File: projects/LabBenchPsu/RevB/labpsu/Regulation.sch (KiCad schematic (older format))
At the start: 19 parts

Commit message: schematic more or less done
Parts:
- IC4: renamed from IC?; footprint SparkFun-SO08 -> (none)
- Q2, Q3: renamed from Q?; footprint TO92 -> (none)
- gave numbers to parts that had none: 15
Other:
- note added: "0-2V V_set \n(for 0-20V V_out)"
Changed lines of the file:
@@
 $EndDescr
 $Comp
-L LT3083 U?
+L LT3083 U9
 U 1 1 57EF9BBB
 P 7075 2450
-F 0 "U?" H 7075 2875 60  0000 C CNN
+F 0 "U9" H 7075 2875 60  0000 C CNN
 F 1 "LT3083" H 7075 2775 60  0000 C CNN
-F 2 "" H 7075 2450 60  0000 C CNN
+F 2 "" H 7075 2450 60  0001 C CNN
 F 3 "" H 7075 2450 60  0000 C CNN
 	1    7075 2450
@@
 NoConn ~ 7650 2325
 $Comp
-L DIODESCH D?
+L DIODESCH D2
 U 1 1 57EF9BC4
 P 7100 1750
-F 0 "D?" H 7100 1850 40  0000 C CNN
+F 0 "D2" H 7100 1850 40  0000 C CNN
 F 1 "SK33A" H 7100 1650 40  0000 C CNN
-F 2 "" H 7100 1750 60  0000 C CNN
+F 2 "" H 7100 1750 60  0001 C CNN
 F 3 "" H 7100 1750 60  0000 C CNN
 	1    7100 1750
@@
 P 4800 3350
 AR Path="/57EF9BF5" Ref="IC?"  Part="1"
-AR Path="/57EF8FB1/57EF9BF5" Ref="IC?"  Part="1"
-F 0 "IC?" H 5125 3250 50  0000 R TNN
+AR Path="/57EF8FB1/57EF9BF5" Ref="IC4"  Part="1"
+F 0 "IC4" H 5125 3250 50  0000 R TNN
 F 1 "LM358" H 4675 3400 50  0000 R TNN
-F 2 "SparkFun-SO08" H 4800 3500 50  0001 C CNN
+F 2 "" H 4800 3500 50  0001 C CNN
 F 3 "" H 4800 3350 60  0000 C CNN
 	1    4800 3350
@@
 P 4900 4425
 AR Path="/57EF9BFC" Ref="IC?"  Part="2"
-AR Path="/57EF8FB1/57EF9BFC" Ref="IC?"  Part="2"
-F 0 "IC?" H 5125 4325 50  0000 R TNN
+AR Path="/57EF8FB1/57EF9BFC" Ref="IC4"  Part="2"
+F 0 "IC4" H 5125 4325 50  0000 R TNN
 F 1 "LM358" H 5200 4575 50  0000 R TNN
-F 2 "SparkFun-SO08" H 4900 4575 50  0001 C CNN
+F 2 "" H 4900 4575 50  0001 C CNN
 F 3 "" H 4900 4425 60  0000 C CNN
 	2    4900 4425
@@
 $EndComp
 $Comp
-L GND #PWR?
+L GND #PWR060
 U 1 1 57EF9C03
 P 4800 3650
-F 0 "#PWR?" H 4800 3650 30  0001 C CNN
+F 0 "#PWR060" H 4800 3650 30  0001 C CNN
 F 1 "GND" H 4800 3580 30  0001 C CNN
 F 2 "" H 4800 3650 60  0000 C CNN
@@
 VSET
 $Comp
-L R R?
+L R R50
 U 1 1 57EF9C0B
 P 4350 2775
-F 0 "R?" V 4430 2775 40  0000 C CNN
+F 0 "R50" V 4430 2775 40  0000 C CNN
 F 1 "18K 0.1%" V 4357 2776 40  0000 C CNN
-F 2 "" V 4280 2775 30  0000 C CNN
+F 2 "" V 4280 2775 30  0001 C CNN
 F 3 "" H 4350 2775 30  0000 C CNN
 	1    4350 2775
@@
 $EndComp
 $Comp
-L R R?
+L R R49
 U 1 1 57EF9C12
 P 4350 2625
-F 0 "R?" V 4430 2625 40  0000 C CNN
+F 0 "R49" V 4430 2625 40  0000 C CNN
 F 1 "18K 0.1%" V 4357 2626 40  0000 C CNN
-F 2 "" V 4280 2625 30  0000 C CNN
+F 2 "" V 4280 2625 30  0001 C CNN
 F 3 "" H 4350 2625 30  0000 C CNN
 	1    4350 2625
@@
 $EndComp
 $Comp
-L R R?
+L R R48
 U 1 1 57EF9C19
 P 3850 2625
-F 0 "R?" V 3930 2625 40  0000 C CNN
+F 0 "R48" V 3930 2625 40  0000 C CNN
 F 1 "1K 0.1%" V 3857 2626 40  0000 C CNN
-F 2 "" V 3780 2625 30  0000 C CNN
+F 2 "" V 3780 2625 30  0001 C CNN
 F 3 "" H 3850 2625 30  0000 C CNN
 	1    3850 2625
@@
 $EndComp
 $Comp
-L GND #PWR?
+L GND #PWR061
 U 1 1 57EF9C20
 P 3600 2725
-F 0 "#PWR?" H 3600 2725 30  0001 C CNN
+F 0 "#PWR061" H 3600 2725 30  0001 C CNN
 F 1 "GND" H 3600 2655 30  0001 C CNN
 F 2 "" H 3600 2725 60  0000 C CNN
@@
 $EndComp
 $Comp
-L R R?
+L R R51
 U 1 1 57EF9C26
 P 5525 3350
-F 0 "R?" V 5605 3350 40  0000 C CNN
+F 0 "R51" V 5605 3350 40  0000 C CNN
 F 1 "1K" V 5532 3351 40  0000 C CNN
-F 2 "" V 5455 3350 30  0000 C CNN
+F 2 "" V 5455 3350 30  0001 C CNN
 F 3 "" H 5525 3350 30  0000 C CNN
 	1    5525 3350
@@
 $EndComp
 $Comp
-L R R?
+L R R54
 U 1 1 57EF9C2D
 P 6325 3350
-F 0 "R?" V 6405 3350 40  0000 C CNN
+F 0 "R54" V 6405 3350 40  0000 C CNN
 F 1 "100R" V 6332 3351 40  0000 C CNN
-F 2 "" V 6255 3350 30  0000 C CNN
+F 2 "" V 6255 3350 30  0001 C CNN
 F 3 "" H 6325 3350 30  0000 C CNN
 	1    6325 3350
@@
 $EndComp
 $Comp
-L R R?
+L R R52
 U 1 1 57EF9C34
 P 5525 3550
-F 0 "R?" V 5605 3550 40  0000 C CNN
+F 0 "R52" V 5605 3550 40  0000 C CNN
 F 1 "10K" V 5532 3551 40  0000 C CNN
-F 2 "" V 5455 3550 30  0000 C CNN
+F 2 "" V 5455 3550 30  0001 C CNN
 F 3 "" H 5525 3550 30  0000 C CNN
 	1    5525 3550
@@
 $EndComp
 $Comp
-L 2N3904 Q?
+L 2N3904 Q2
 U 1 1 57EF9C3B
 P 5975 3550
-F 0 "Q?" H 5975 3401 40  0000 R CNN
+F 0 "Q2" H 5975 3401 40  0000 R CNN
 F 1 "2N3904" H 6400 3550 40  0000 R CNN
-F 2 "TO92" H 5875 3652 29  0000 C CNN
+F 2 "" H 5875 3652 29  0001 C CNN
 F 3 "" H 5975 3550 60  0000 C CNN
 	1    5975 3550
@@
 $EndComp
 $Comp
-L GND #PWR?
+L GND #PWR062
 U 1 1 57EF9C42
 P 6075 3750
-F 0 "#PWR?" H 6075 3750 30  0001 C CNN
+F 0 "#PWR062" H 6075 3750 30  0001 C CNN
 F 1 "GND" H 6075 3680 30  0001 C CNN
 F 2 "" H 6075 3750 60  0000 C CNN
@@
 $EndComp
 $Comp
-L C C?
+L C C25
 U 1 1 57EF9C73
 P 5025 2975
-F 0 "C?" H 5025 3075 40  0000 L CNN
+F 0 "C25" H 5025 3075 40  0000 L CNN
 F 1 "100nF" H 5031 2890 40  0000 L CNN
-F 2 "" H 5063 2825 30  0000 C CNN
+F 2 "" H 5063 2825 30  0001 C CNN
 F 3 "" H 5025 2975 60  0000 C CNN
 	1    5025 2975
@@
 $EndComp
 $Comp
-L GND #PWR?
+L GND #PWR063
 U 1 1 57EF9C7A
 P 5025 3175
-F 0 "#PWR?" H 5025 3175 30  0001 C CNN
+F 0 "#PWR063" H 5025 3175 30  0001 C CNN
 F 1 "GND" H 5025 3105 30  0001 C CNN
 F 2 "" H 5025 3175 60  0000 C CNN
@@
 $EndComp
 $Comp
-L R R?
+L R R53
 U 1 1 57EF9C81
 P 5525 4425
-F 0 "R?" V 5605 4425 40  0000 C CNN
+F 0 "R53" V 5605 4425 40  0000 C CNN
 F 1 "10K" V 5532 4426 40  0000 C CNN
-F 2 "" V 5455 4425 30  0000 C CNN
+F 2 "" V 5455 4425 30  0001 C CNN
 F 3 "" H 5525 4425 30  0000 C CNN
 	1    5525 4425
@@
 $EndComp
 $Comp
-L 2N3904 Q?
+L 2N3904 Q3
 U 1 1 57EF9C88
 P 5975 4425
-F 0 "Q?" H 5975 4276 40  0000 R CNN
+F 0 "Q3" H 5975 4276 40  0000 R CNN
 F 1 "2N3904" H 6400 4425 40  0000 R CNN
-F 2 "TO92" H 5875 4527 29  0000 C CNN
+F 2 "" H 5875 4527 29  0001 C CNN
 F 3 "" H 5975 4425 60  0000 C CNN
 	1    5975 4425
@@
 $EndComp
 $Comp
-L GND #PWR?
+L GND #PWR064
 U 1 1 57EF9C8F
 P 6075 4625
-F 0 "#PWR?" H 6075 4625 30  0001 C CNN
+F 0 "#PWR064" H 6075 4625 30  0001 C CNN
 F 1 "GND" H 6075 4555 30  0001 C CNN
 F 2 "" H 6075 4625 60  0000 C CNN
@@
 Clim
 $Comp
-L C C?
+L C C26
 U 1 1 57EF9C97
 P 7075 3550
-F 0 "C?" H 7075 3650 40  0000 L CNN
+F 0 "C26" H 7075 3650 40  0000 L CNN
 F 1 "22uF" H 7081 3465 40  0000 L CNN
-F 2 "" H 7113 3400 30  0000 C CNN
+F 2 "" H 7113 3400 30  0001 C CNN
 F 3 "" H 7075 3550 60  0000 C CNN
 	1    7075 3550
@@
 $EndComp
 $Comp
-L C C?
+L C C27
 U 1 1 57EF9C9E
 P 7825 3550
-F 0 "C?" H 7825 3650 40  0000 L CNN
+F 0 "C27" H 7825 3650 40  0000 L CNN
 F 1 "2u2F" H 7831 3465 40  0000 L CNN
-F 2 "" H 7863 3400 30  0000 C CNN
+F 2 "" H 7863 3400 30  0001 C CNN
 F 3 "" H 7825 3550 60  0000 C CNN
 	1    7825 3550
@@
 $EndComp
 $Comp
-L DIODESCH D?
+L DIODESCH D3
 U 1 1 57EF9CA5
 P 8650 2450
-F 0 "D?" H 8650 2550 40  0000 C CNN
+F 0 "D3" H 8650 2550 40  0000 C CNN
 F 1 "SK33A" H 8650 2350 40  0000 C CNN
-F 2 "" H 8650 2450 60  0000 C CNN
+F 2 "" H 8650 2450 60  0001 C CNN
 F 3 "" H 8650 2450 60  0000 C CNN
 	1    8650 2450
@@
 $EndComp
 $Comp
-L LM334Z U?
+L LM334Z U10
 U 1 1 57EF9CAC
 P 8275 3000
-F 0 "U?" H 8275 3225 60  0000 C CNN
+F 0 "U10" H 8275 3225 60  0000 C CNN
 F 1 "LM334Z" H 8275 3125 60  0000 C CNN
-F 2 "" H 8275 2900 60  0000 C CNN
+F 2 "" H 8275 2900 60  0001 C CNN
 F 3 "" H 8275 2900 60  0000 C CNN
 	1    8275 3000
@@
 $EndComp
 $Comp
-L R R?
+L R R55
 U 1 1 57EF9CB3
 P 8650 3375
-F 0 "R?" V 8730 3375 40  0000 C CNN
+F 0 "R55" V 8730 3375 40  0000 C CNN
 F 1 "100R" V 8657 3376 40  0000 C CNN
-F 2 "" V 8580 3375 30  0000 C CNN
+F 2 "" V 8580 3375 30  0001 C CNN
 F 3 "" H 8650 3375 30  0000 C CNN
 	1    8650 3375
@@
 $EndComp
 $Comp
-L GND #PWR?
+L GND #PWR065
 U 1 1 57EF9CBA
 P 8650 2650
-F 0 "#PWR?" H 8650 2650 30  0001 C CNN
+F 0 "#PWR065" H 8650 2650 30  0001 C CNN
 F 1 "GND" H 8650 2580 30  0001 C CNN
 F 2 "" H 8650 2650 60  0000 C CNN
@@
 constant current \ndrain of 677uA
 $Comp
-L GND #PWR?
+L GND #PWR066
 U 1 1 57EF9CC8
 P 7825 3875
-F 0 "#PWR?" H 7825 3875 30  0001 C CNN
+F 0 "#PWR066" H 7825 3875 30  0001 C CNN
 F 1 "GND" H 7825 3805 30  0001 C CNN
 F 2 "" H 7825 3875 60  0000 C CNN
@@
 	6900 1750 6500 1750
 Wire Wire Line
-	6500 2250 6500 1750
+	6500 1750 6500 2250
 Wire Wire Line
 	1550 3450 4600 3450
@@
 Connection ~ 6575 3350
 Wire Wire Line
-	1550 2250 6500 2250
+	6500 2250 1550 2250
 Wire Wire Line
 	3600 2625 3600 2725
@@
 Wire Wire Line
 	4600 4325 1550 4325
+Text Notes 1350 3275 0    60   ~ 0
+0-2V V_set \n(for 0-20V V_out)
 $EndSCHEMATC

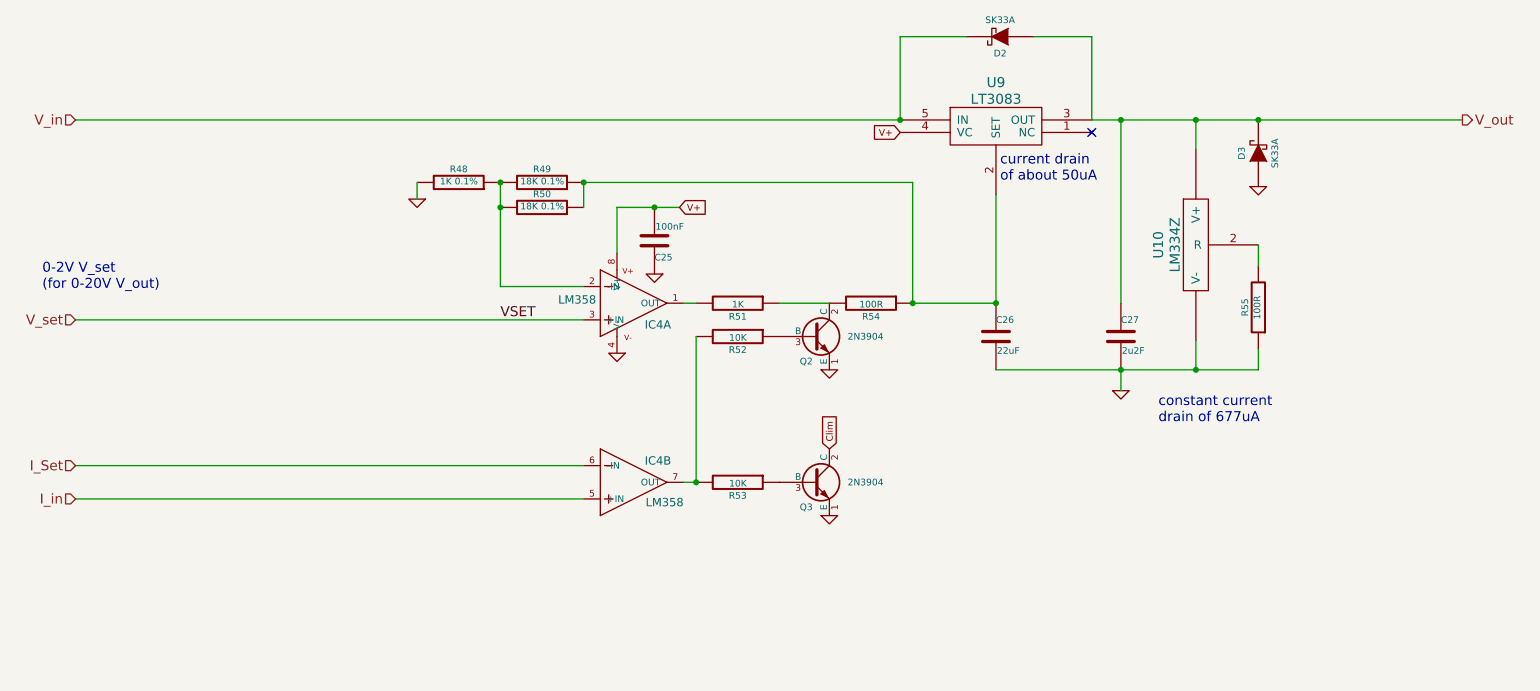
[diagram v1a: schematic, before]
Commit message: schematic with new DAC
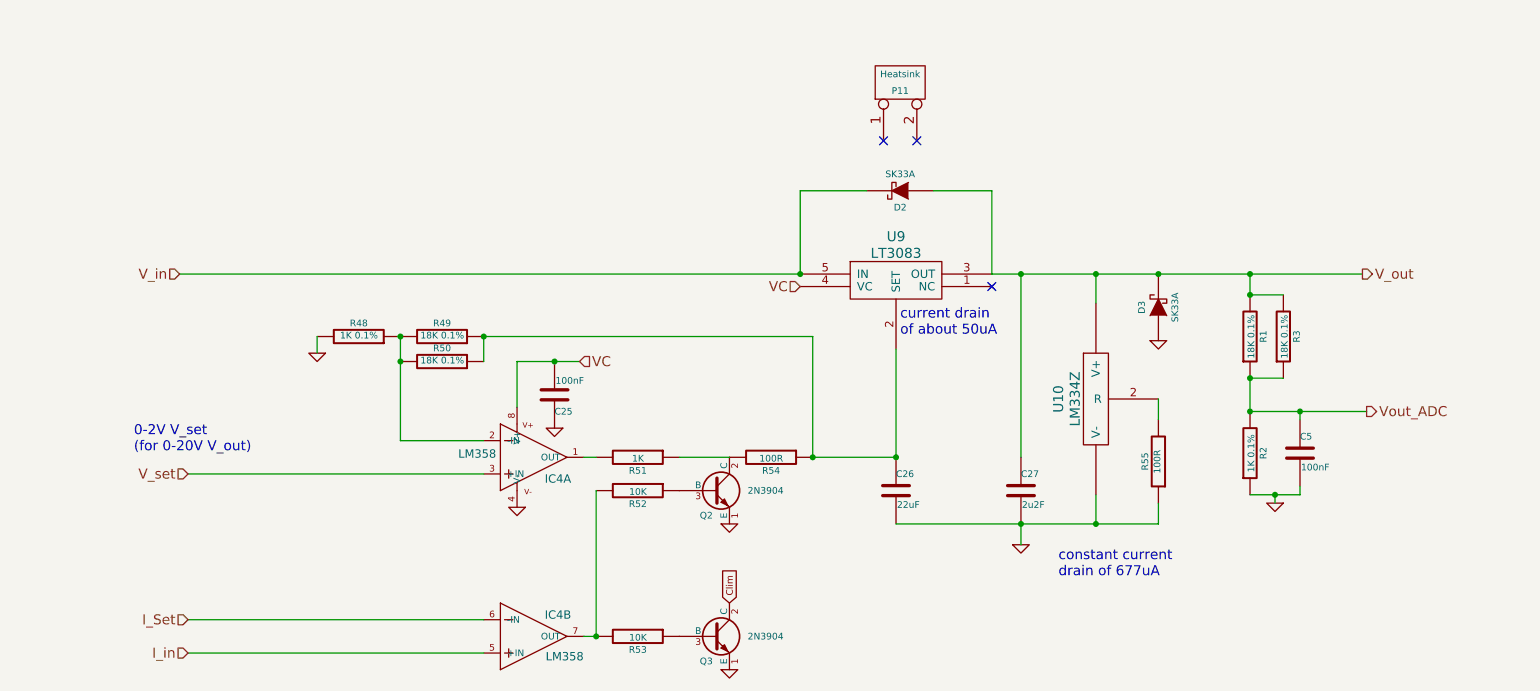
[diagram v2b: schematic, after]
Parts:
- added C5: 100nF, symbol C
- added P11: Heatsink, symbol CONN_2
- added R1, R3: 18K 0.1%, symbol R
- added R2: 1K 0.1%, symbol R
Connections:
- net GND: now also C5.2, R2.1
- net V_out: now also R1.2, R3.2
- net V+ renamed VC
- new net Vout_ADC: C5.1, R1.1, R2.2, R3.1
- no-connect marks 1 -> 3
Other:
- moved on the sheet: C25, C26, C27, D2, D3, IC4A, IC4B, Q2, Q3, R48, R49, R50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
